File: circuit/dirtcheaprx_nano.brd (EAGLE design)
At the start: 19.6 x 24.4 mm, 22 parts, among them IC1 MCP1700

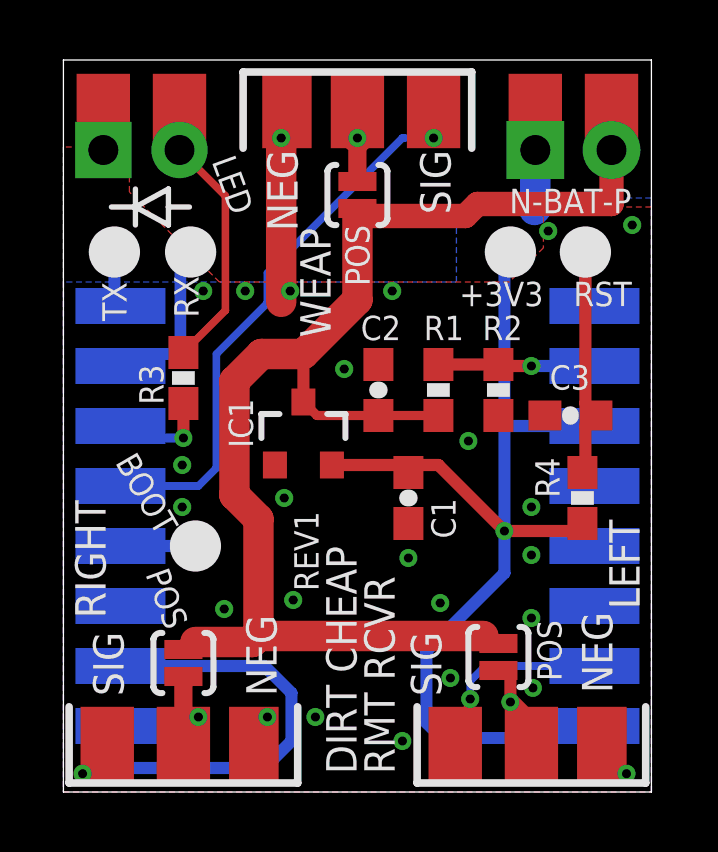
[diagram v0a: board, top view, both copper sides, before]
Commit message: moved right servo sig trace above danger zone
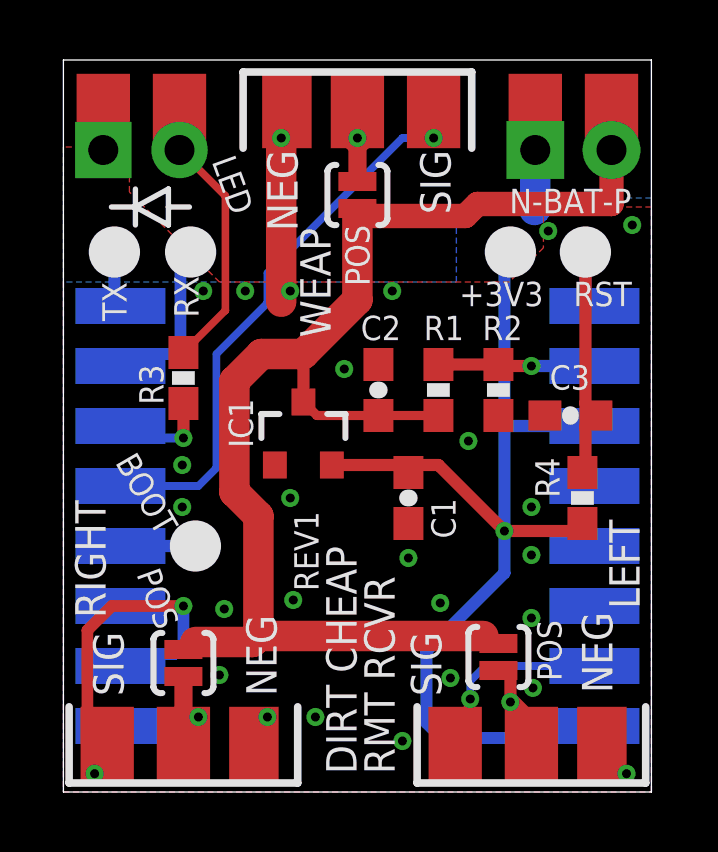
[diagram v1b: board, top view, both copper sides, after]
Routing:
- net SIG-RIGHT: track 16.7 -> 13.1 mm, vias 1 -> 2
- net GND: vias 25 -> 26
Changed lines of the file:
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@@
 <layer number="21" name="tPlace" color="7" fill="1" visible="yes" active="yes"/>
 <layer number="22" name="bPlace" color="7" fill="1" visible="yes" active="yes"/>
-<layer number="23" name="tOrigins" color="15" fill="1" visible="yes" active="yes"/>
-<layer number="24" name="bOrigins" color="15" fill="1" visible="yes" active="yes"/>
+<layer number="23" name="tOrigins" color="15" fill="1" visible="no" active="yes"/>
+<layer number="24" name="bOrigins" color="15" fill="1" visible="no" active="yes"/>
 <layer number="25" name="tNames" color="7" fill="1" visible="yes" active="yes"/>
 <layer number="26" name="bNames" color="7" fill="1" visible="yes" active="yes"/>
@@
 <text x="1.5" y="3.2" size="1.016" layer="21" ratio="10" rot="R90" align="center-left">SIG</text>
 <text x="6.6" y="3.2" size="1.016" layer="21" ratio="10" rot="R90" align="center-left">NEG</text>
-<text x="3.8" y="5.5" size="0.8128" layer="21" ratio="10" rot="R110" align="center-left">POS</text>
+<text x="3.5" y="5.5" size="0.8128" layer="21" ratio="10" rot="R110" align="center-left">POS</text>
 <text x="7.3" y="21.4" size="1.016" layer="21" ratio="10" rot="R270" align="center-left">NEG</text>
 <text x="12.4" y="21.4" size="1.016" layer="21" ratio="10" rot="R270" align="center-left">SIG</text>
@@
 RMT RCVR</text>
 <text x="8.1" y="6.7" size="0.8128" layer="21" ratio="10" distance="25" rot="R90" align="center-left">REV1</text>
+<wire x1="4.3" y1="7.3" x2="4.3" y2="6.6" width="0" layer="42"/>
 </plain>
 <attributes>
@@
 <wire x1="8" y1="14.6" x2="6.6" y2="14.6" width="1.016" layer="1"/>
 <wire x1="6.6" y1="14.6" x2="5.7" y2="13.7" width="1.016" layer="1"/>
-<wire x1="5.7" y1="13.7" x2="5.7" y2="9.9" width="1.016" layer="1"/>
-<wire x1="5.7" y1="9.9" x2="6.5" y2="9.1" width="1.016" layer="1"/>
-<wire x1="6.5" y1="9.1" x2="6.5" y2="5.2" width="1.016" layer="1"/>
+<wire x1="5.7" y1="13.7" x2="5.7" y2="10" width="1.016" layer="1"/>
+<wire x1="5.7" y1="10" x2="6.5" y2="9.2" width="1.016" layer="1"/>
+<wire x1="6.5" y1="9.2" x2="6.5" y2="5.2" width="1.016" layer="1"/>
 <wire x1="8" y1="13" x2="8" y2="14.6" width="0.4064" layer="1"/>
 <wire x1="9.8" y1="19.45" x2="9.8" y2="19.3" width="0.254" layer="1"/>
@@
 <via x="4.66" y="16.7" extent="1-16" drill="0.3" shape="octagon"/>
 <via x="6.06" y="16.7" extent="1-16" drill="0.3" shape="octagon"/>
-<via x="7.36" y="9.8" extent="1-16" drill="0.3" shape="octagon"/>
+<via x="7.56" y="9.8" extent="1-16" drill="0.3" shape="octagon"/>
 <via x="9.36" y="14.1" extent="1-16" drill="0.3" shape="octagon"/>
 <via x="10.96" y="16.7" extent="1-16" drill="0.3" shape="octagon"/>
@@
 <via x="3.96" y="10.9" extent="1-16" drill="0.3" shape="octagon"/>
 <via x="3.96" y="9.5" extent="1-16" drill="0.3" shape="octagon"/>
+<via x="5.2" y="3.9" extent="1-16" drill="0.3" shape="octagon"/>
 </signal>
 <signal name="ADC">
@@
 <contactref element="U1" pad="GPIO15"/>
 <contactref element="SERVO2" pad="SIG"/>
-<via x="0.64" y="0.61" extent="1-16" drill="0.3" shape="square"/>
-<wire x1="6.7" y1="0.8" x2="7.6" y2="1.7" width="0.4064" layer="16"/>
-<wire x1="7.6" y1="1.7" x2="7.6" y2="3.3" width="0.4064" layer="16"/>
-<wire x1="7.6" y1="3.3" x2="6.7" y2="4.2" width="0.4064" layer="16"/>
-<wire x1="6.7" y1="4.2" x2="1.9" y2="4.2" width="0.4064" layer="16"/>
-<wire x1="1.46" y1="1.57" x2="1.14" y2="1.25" width="0.254" layer="1"/>
-<wire x1="1.14" y1="1.25" x2="1.14" y2="0.61" width="0.6096" layer="1"/>
-<wire x1="1.14" y1="0.61" x2="0.64" y2="0.61" width="0.6096" layer="1"/>
-<wire x1="6.7" y1="0.8" x2="0.83" y2="0.8" width="0.4064" layer="16"/>
-<wire x1="0.83" y1="0.8" x2="0.64" y2="0.61" width="0.4064" layer="16"/>
+<via x="1.04" y="0.61" extent="1-16" drill="0.3" shape="square"/>
+<wire x1="1.9" y1="4.2" x2="2.3" y2="4.6" width="0.39" layer="16"/>
+<wire x1="2.3" y1="4.6" x2="3.7" y2="4.6" width="0.39" layer="16"/>
+<wire x1="3.7" y1="4.6" x2="4" y2="4.9" width="0.39" layer="16"/>
+<wire x1="4" y1="4.9" x2="4" y2="6.2" width="0.39" layer="16"/>
+<via x="4" y="6.2" extent="1-16" drill="0.3" shape="octagon"/>
+<wire x1="0.8" y1="1.57" x2="1.46" y2="1.57" width="0.39" layer="1"/>
+<wire x1="4" y1="6.2" x2="1.6099" y2="6.2" width="0.39" layer="1"/>
+<wire x1="1.6099" y1="6.2" x2="0.8" y2="5.3901" width="0.39" layer="1"/>
+<wire x1="0.8" y1="5.3901" x2="0.8" y2="1.57" width="0.39" layer="1"/>
+<wire x1="1.04" y1="0.61" x2="1.46" y2="0.61" width="0.39" layer="1"/>
+<wire x1="1.46" y1="0.61" x2="1.46" y2="1.57" width="0.39" layer="1"/>
 </signal>
 <signal name="N$8">

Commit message: GPIO15 needs to be pulled down, I missed the memo...
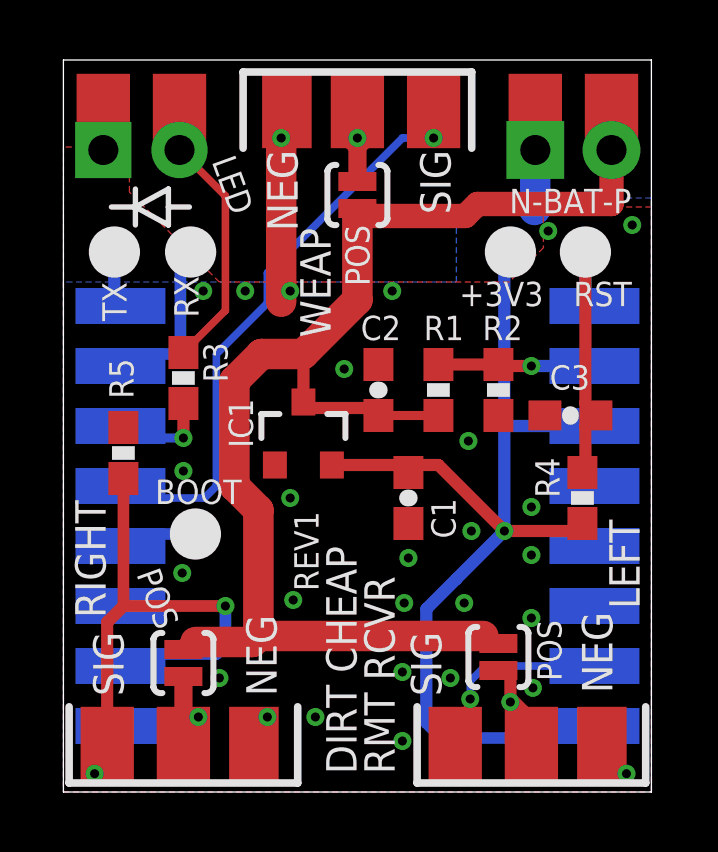
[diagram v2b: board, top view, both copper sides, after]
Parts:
- added R5: 7K5Ω, dirtcheaprx_nano:0603-RES
- moved TP4 0.40 mm to (4.40, 8.60)
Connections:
- net GND: now also R5.1
- net SIG-RIGHT: now also R5.2
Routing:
- net SIG-RIGHT: track 13.1 -> 19.0 mm
- net SIG-WEAP: track 19.0 -> 19.9 mm
- net GND: vias 26 -> 28

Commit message: corrected GPIO4 and GPIO5 mixup in PCBs
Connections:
- net LED: now also U1.GPIO5; no longer U1.GPIO4
- net SIG-WEAP: now also U1.GPIO4; no longer U1.GPIO5
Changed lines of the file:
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@@
 </signal>
 <signal name="LED">
-<contactref element="U1" pad="GPIO4"/>
+<contactref element="U1" pad="GPIO5"/>
 <contactref element="R3" pad="1"/>
 <via x="4" y="11.8" extent="1-16" drill="0.3" shape="octagon"/>
@@
 </signal>
 <signal name="SIG-WEAP">
-<contactref element="U1" pad="GPIO5"/>
+<contactref element="U1" pad="GPIO4"/>
 <contactref element="SERVO1" pad="SIG"/>
 <via x="12.34" y="21.8" extent="1-16" drill="0.3" shape="square"/>

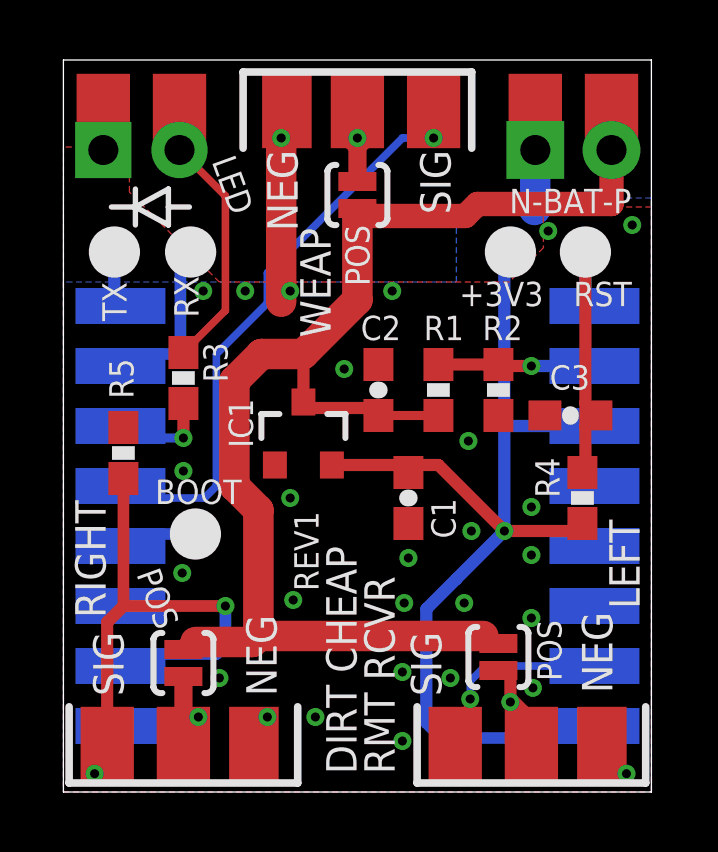
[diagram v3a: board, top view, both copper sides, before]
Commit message: better battery reading
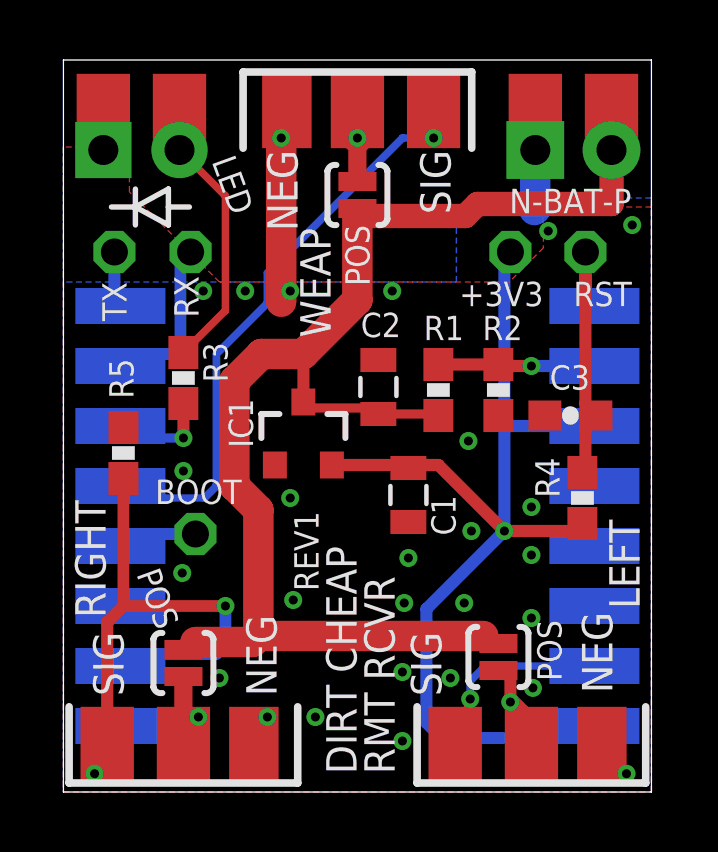
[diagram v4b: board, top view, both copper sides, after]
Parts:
- C1: value 100uF -> 4u7; device dirtcheaprx_nano:0603-CAP -> dirtcheaprx_nano:0805
- C2: value 1u -> 22u; device dirtcheaprx_nano:0603-CAP -> dirtcheaprx_nano:0805
- C3: value 100uF -> 100n
- IC1: value MCP1700 -> MCP1703T-3302E/CB
- R1, R4, R5: value 7K5Ω -> 5K6Ω
- R2: value 1KΩ -> 470Ω
- moved C1 0.10 mm to (11.5, 9.90)
- moved C2 0.10 mm to (10.5, 13.5)
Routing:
- net GND: vias 28 -> 27
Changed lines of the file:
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@@
 <layer number="16" name="Bottom" color="1" fill="1" visible="yes" active="yes"/>
 <layer number="17" name="Pads" color="2" fill="1" visible="yes" active="yes"/>
-<layer number="18" name="Vias" color="2" fill="1" visible="yes" active="yes"/>
+<layer number="18" name="Vias" color="14" fill="1" visible="yes" active="yes"/>
 <layer number="19" name="Unrouted" color="6" fill="1" visible="yes" active="yes"/>
 <layer number="20" name="Dimension" color="15" fill="1" visible="yes" active="yes"/>
@@
 <layer number="37" name="tTest" color="7" fill="1" visible="no" active="yes"/>
 <layer number="38" name="bTest" color="7" fill="1" visible="no" active="yes"/>
-<layer number="39" name="tKeepout" color="4" fill="11" visible="yes" active="yes"/>
-<layer number="40" name="bKeepout" color="1" fill="11" visible="yes" active="yes"/>
-<layer number="41" name="tRestrict" color="4" fill="10" visible="yes" active="yes"/>
-<layer number="42" name="bRestrict" color="1" fill="10" visible="yes" active="yes"/>
+<layer number="39" name="tKeepout" color="4" fill="11" visible="no" active="yes"/>
+<layer number="40" name="bKeepout" color="1" fill="11" visible="no" active="yes"/>
+<layer number="41" name="tRestrict" color="4" fill="10" visible="no" active="yes"/>
+<layer number="42" name="bRestrict" color="1" fill="10" visible="no" active="yes"/>
 <layer number="43" name="vRestrict" color="2" fill="10" visible="no" active="yes"/>
 <layer number="44" name="Drills" color="7" fill="1" visible="no" active="yes"/>
@@
 <text x="9.8" y="18.9" size="0.8128" layer="21" ratio="10" rot="R270" align="center-left">POS</text>
 <text x="16.9" y="19.7" size="0.8128" layer="21" ratio="10" align="center">N-BAT-P</text>
-<text x="10.6" y="11" size="1.016" layer="22" ratio="10" rot="MR0" align="center">DIRT
+<text x="13.5" y="12.6" size="1.016" layer="22" ratio="10" rot="MR0" align="center">DIRT
 CHEAP
 RC RX</text>
-<text x="8.3" y="7.9" size="1.016" layer="22" ratio="10" rot="MR0" align="center">REV-1</text>
+<text x="12.9" y="9.7" size="1.016" layer="22" ratio="10" rot="MR0" align="center">REV-1</text>
 <wire x1="15.7" y1="18" x2="19.4" y2="18" width="0" layer="42"/>
 <wire x1="7.6" y1="12.6" x2="6.2" y2="12.6" width="0" layer="41"/>
-<wire x1="11" y1="13.7" x2="12" y2="13.7" width="0" layer="41"/>
+<wire x1="10" y1="13.7" x2="12" y2="13.7" width="0" layer="41"/>
 <wire x1="13" y1="13.1" x2="14" y2="13.1" width="0" layer="41"/>
 <wire x1="15.5" y1="13.2" x2="15.5" y2="13.8" width="0" layer="41"/>
@@
 <text x="8.1" y="6.7" size="0.8128" layer="21" ratio="10" distance="25" rot="R90" align="center-left">REV1</text>
 <wire x1="1.5" y1="11.6" x2="0.3" y2="11.6" width="0" layer="41"/>
+<wire x1="3.4" y1="3.6" x2="3.4" y2="2.8" width="0" layer="42"/>
+<wire x1="3.4" y1="2.8" x2="3.39" y2="2.8" width="0" layer="42"/>
+<wire x1="1.69" y1="2.8" x2="2.11" y2="2.8" width="0" layer="42"/>
+<wire x1="10.9" y1="10.4" x2="10.9" y2="9.4" width="0" layer="41"/>
+<wire x1="10.9" y1="9.4" x2="12.1" y2="9.4" width="0" layer="41"/>
+<wire x1="12.1" y1="9.4" x2="12.1" y2="10.4" width="0" layer="41"/>
+<wire x1="9.9" y1="13" x2="9.9" y2="15.6" width="0" layer="41"/>
 </plain>
 <attributes>
@@
 <attribute name="VALUE" x="17.5" y="-1.3" size="1.4224" layer="28" rot="MR0"/>
 </element>
-<element name="R1" library="dirtcheaprx_nano" package="0603-RES" value="7K5Ω" x="12.5" y="13.4" smashed="yes" rot="R270">
+<element name="R1" library="dirtcheaprx_nano" package="0603-RES" value="5K6Ω" x="12.5" y="13.4" smashed="yes" rot="R270">
 <attribute name="NAME" x="12.011" y="15.062" size="0.8128" layer="25" font="vector"/>
 </element>
-<element name="R2" library="dirtcheaprx_nano" package="0603-RES" value="1KΩ" x="14.5" y="13.4" smashed="yes" rot="R90">
+<element name="R2" library="dirtcheaprx_nano" package="0603-RES" value="470Ω" x="14.5" y="13.4" smashed="yes" rot="R90">
 <attribute name="NAME" x="13.971" y="15.062" size="0.8128" layer="25" font="vector"/>
 </element>
@@
 <element name="SERVO2" library="dirtcheaprx_nano" package="SERVO-EDGE" value="SERVO-SMD-EDGE-1" x="4" y="0.3" locked="yes" smashed="yes"/>
 <element name="SERVO3" library="dirtcheaprx_nano" package="SERVO-EDGE" value="SERVO-SMD-EDGE-1" x="15.6" y="0.3" locked="yes" smashed="yes"/>
-<element name="IC1" library="dirtcheaprx_nano" package="SOT23-3" value="MCP1700" x="8" y="11.9" smashed="yes">
+<element name="IC1" library="dirtcheaprx_nano" package="SOT23-3" value="MCP1703T-3302E/CB" x="8" y="11.9" smashed="yes">
 <attribute name="NAME" x="6.322" y="11.4745" size="0.8128" layer="25" rot="R90"/>
-<attribute name="VALUE" x="6.984" y="11.7095" size="0.4064" layer="27"/>
-</element>
-<element name="C1" library="dirtcheaprx_nano" package="0603-CAP" value="100uF" x="11.5" y="9.8" smashed="yes" rot="R270">
-<attribute name="NAME" x="12.262" y="9.789" size="0.8128" layer="25" font="vector" rot="R270"/>
-</element>
-<element name="C2" library="dirtcheaprx_nano" package="0603-CAP" value="1u" x="10.5" y="13.4" smashed="yes" rot="R90">
-<attribute name="NAME" x="9.911" y="15.062" size="0.8128" layer="25" font="vector"/>
+</element>
+<element name="C1" library="dirtcheaprx_nano" package="0805" value="4u7" x="11.5" y="9.9" smashed="yes" rot="R270">
+<attribute name="NAME" x="12.262" y="9.889" size="0.8128" layer="25" font="vector" rot="R270"/>
+</element>
+<element name="C2" library="dirtcheaprx_nano" package="0805" value="22u" x="10.5" y="13.5" smashed="yes" rot="R90">
+<attribute name="NAME" x="9.911" y="15.162" size="0.8128" layer="25" font="vector"/>
 </element>
 <element name="SJ1" library="dirtcheaprx_nano" package="SJ_2S-NO" value="" x="9.8" y="19.9" locked="yes" smashed="yes" rot="R270">
@@
 <attribute name="TP_SIGNAL_NAME" value="" x="16.17" y="15.46" size="1" layer="38" rot="MR0"/>
 </element>
-<element name="C3" library="dirtcheaprx_nano" package="0603-CAP" value="100uF" x="16.9" y="12.55" smashed="yes">
+<element name="C3" library="dirtcheaprx_nano" package="0603-CAP" value="100n" x="16.9" y="12.55" smashed="yes">
 <attribute name="NAME" x="16.211" y="13.412" size="0.8128" layer="25" font="vector"/>
-<attribute name="VALUE" x="15.884" y="11.407" size="0.4064" layer="27" font="vector"/>
-</element>
-<element name="R4" library="dirtcheaprx_nano" package="0603-RES" value="7K5Ω" x="17.3" y="9.8" smashed="yes" rot="R270">
+</element>
+<element name="R4" library="dirtcheaprx_nano" package="0603-RES" value="5K6Ω" x="17.3" y="9.8" smashed="yes" rot="R270">
 <attribute name="NAME" x="16.538" y="9.811" size="0.8128" layer="25" font="vector" rot="R90"/>
-<attribute name="VALUE" x="16.157" y="10.816" size="0.4064" layer="27" font="vector" rot="R270"/>
-</element>
-<element name="R5" library="dirtcheaprx_nano" package="0603-RES" value="7K5Ω" x="2" y="11.3" smashed="yes" rot="R270">
+</element>
+<element name="R5" library="dirtcheaprx_nano" package="0603-RES" value="5K6Ω" x="2" y="11.3" smashed="yes" rot="R270">
 <attribute name="NAME" x="2.338" y="13.111" size="0.8128" layer="25" font="vector" ratio="10" rot="R90"/>
-<attribute name="VALUE" x="0.857" y="12.316" size="0.4064" layer="27" font="vector" rot="R270"/>
 </element>
 </elements>
@@
 <wire x1="14.7" y1="17.8" x2="14.9" y2="18" width="0.4064" layer="16"/>
 <wire x1="14.7" y1="12.2" x2="14.7" y2="8.7" width="0.4064" layer="16"/>
-<wire x1="14.7" y1="8.7" x2="13.1" y2="7.1" width="0.4064" layer="16"/>
-<wire x1="13.1" y1="7.1" x2="12.1" y2="6.1" width="0.4064" layer="16"/>
+<wire x1="14.7" y1="8.7" x2="12.1" y2="6.1" width="0.4064" layer="16"/>
 <wire x1="12.1" y1="6.1" x2="12.1" y2="2.3" width="0.4064" layer="16"/>
 <wire x1="8.95" y1="10.9" x2="11.5" y2="10.9" width="0.4064" layer="1"/>
-<wire x1="11.5" y1="10.9" x2="11.5" y2="10.65" width="0.4064" layer="1"/>
-<wire x1="11.5" y1="10.65" x2="11.8" y2="10.85" width="0.4064" layer="1"/>
+<wire x1="11.5" y1="10.9" x2="11.5" y2="10.8" width="0.4064" layer="1"/>
+<wire x1="11.5" y1="10.8" x2="11.8" y2="10.85" width="0.4064" layer="1"/>
 <wire x1="11.8" y1="10.85" x2="11.8" y2="10.9" width="0.4064" layer="1"/>
 <wire x1="11.8" y1="10.9" x2="12.5" y2="10.9" width="0.4064" layer="1"/>
@@
 <wire x1="4.4" y1="5" x2="4.35" y2="5.1" width="0.6096" layer="1"/>
 <wire x1="4.35" y1="5.1" x2="4" y2="4.75" width="0.6096" layer="1"/>
-<wire x1="10.5" y1="12.55" x2="12.5" y2="12.55" width="0.3048" layer="1"/>
 <wire x1="18.27" y1="21.4" x2="18.27" y2="19.6" width="0.8128" layer="1"/>
 <wire x1="18.27" y1="19.6" x2="13.8" y2="19.6" width="0.8128" layer="1"/>
@@
 <wire x1="9.8" y1="19.3" x2="9.9" y2="19.2" width="0.254" layer="1"/>
 <wire x1="8" y1="13" x2="8.2" y2="12.8" width="0.4064" layer="1"/>
-<wire x1="8.2" y1="12.8" x2="10.5" y2="12.8" width="0.4064" layer="1"/>
-<wire x1="10.5" y1="12.8" x2="10.5" y2="12.55" width="0.4064" layer="1"/>
+<wire x1="8.2" y1="12.8" x2="10.2" y2="12.8" width="0.3048" layer="1"/>
+<wire x1="10.2" y1="12.8" x2="10.5" y2="12.6" width="0.3048" layer="1"/>
+<wire x1="12.45" y1="12.5" x2="12.5" y2="12.55" width="0.3048" layer="1"/>
+<wire x1="10.5" y1="12.6" x2="12.45" y2="12.6" width="0.3048" layer="1"/>
+<wire x1="12.45" y1="12.6" x2="12.5" y2="12.55" width="0.3048" layer="1"/>
 </signal>
 <signal name="GND">
@@
 <via x="6.06" y="16.7" extent="1-16" drill="0.3" shape="octagon"/>
 <via x="7.56" y="9.8" extent="1-16" drill="0.3" shape="octagon"/>
-<via x="9.36" y="14.1" extent="1-16" drill="0.3" shape="octagon"/>
 <via x="10.96" y="16.7" extent="1-16" drill="0.3" shape="octagon"/>
 <via x="15.65" y="3.47" extent="1-16" drill="0.3" shape="octagon"/>
